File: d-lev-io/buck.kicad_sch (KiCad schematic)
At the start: 13 parts, among them U3 TPS54202DDC

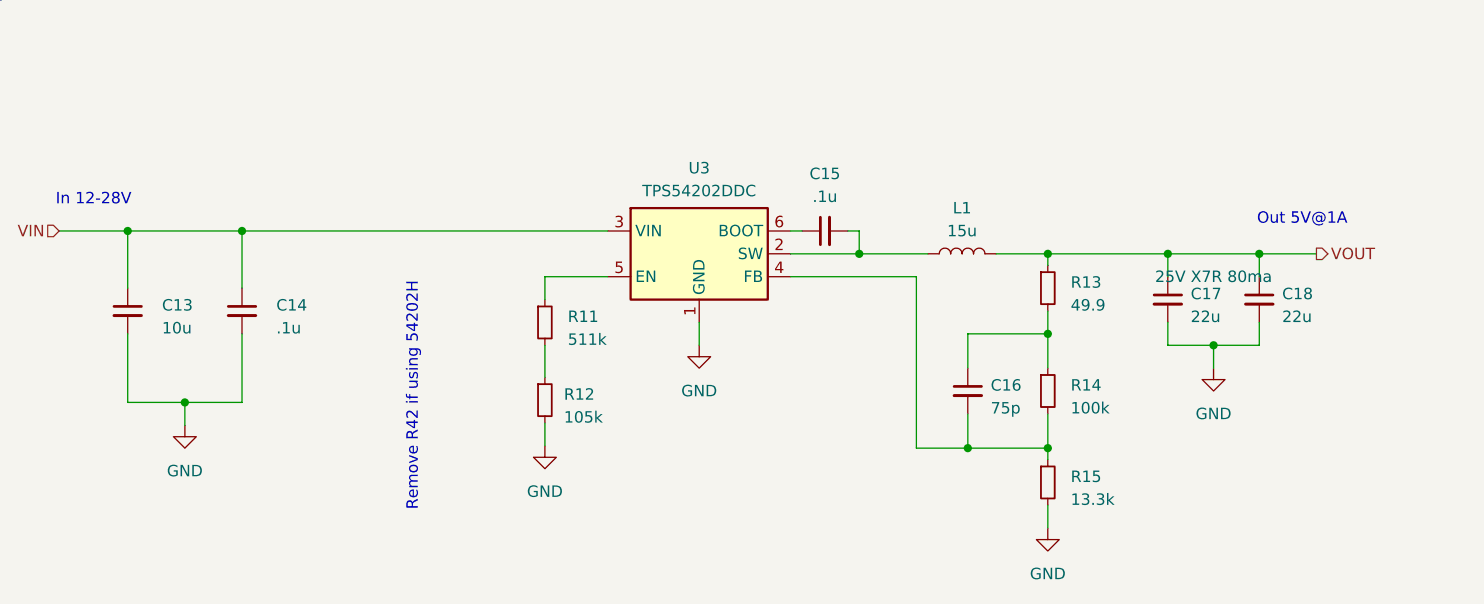
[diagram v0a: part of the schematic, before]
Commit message: I/O board silk placement
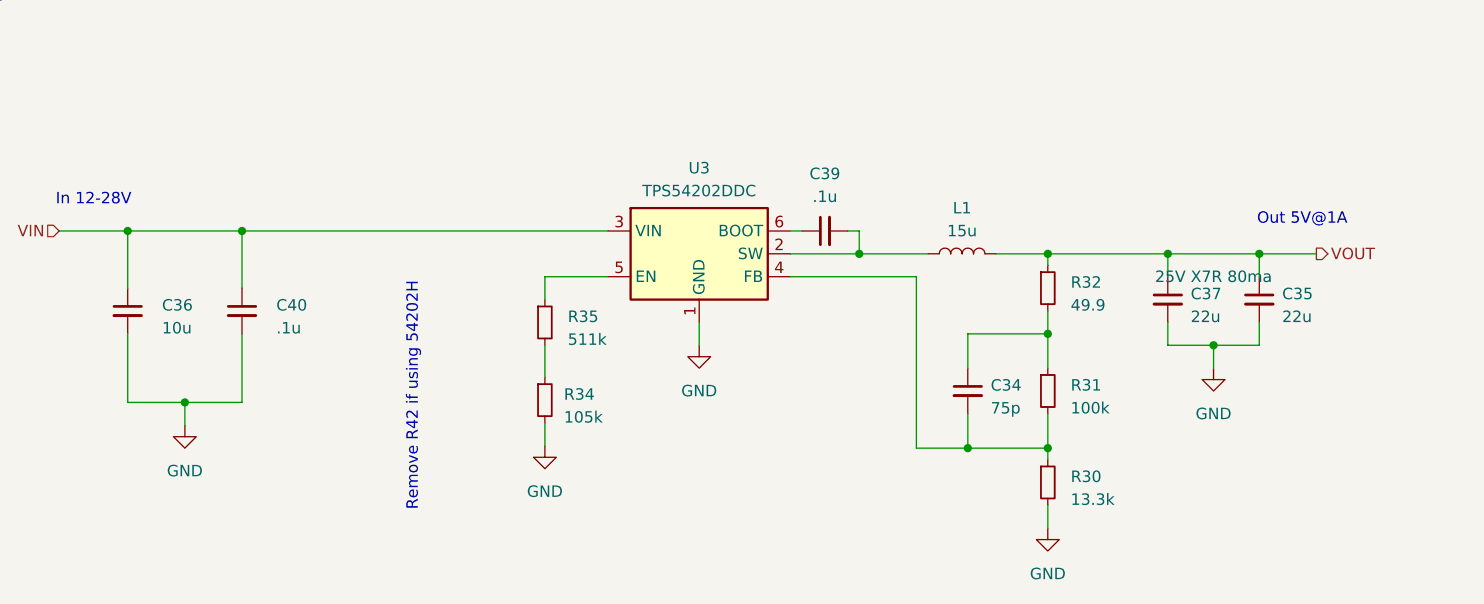
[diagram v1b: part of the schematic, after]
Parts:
- renumbered C16 to C34, C18 to C35, C13 to C36, C17 to C37, C15 to C39, C14 to C40, R15 to R30, R14 to R31, R13 to R32, R12 to R34, R11 to R35
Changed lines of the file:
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@@
   (symbol (lib_id "Device:R_Small") (at 193.675 110.49 0) (unit 1)
     (in_bom yes) (on_board yes) (dnp no) (fields_autoplaced)
-    (property "Reference" "R15" (at 196.215 109.855 0)
+    (property "Reference" "R30" (at 196.215 109.855 0)
       (effects (font (size 1.27 1.27)) (justify left))
     )
@@
       (project "d-lev-io"
         (path "/9261a07b-ae4a-4d72-8042-ea097cd0e5ed/f19ba83a-ef5a-459f-9ba4-5cb53e267077"
-          (reference "R15") (unit 1)
+          (reference "R30") (unit 1)
         )
       )
@@
   (symbol (lib_id "Device:R_Small") (at 193.675 88.9 0) (unit 1)
     (in_bom yes) (on_board yes) (dnp no) (fields_autoplaced)
-    (property "Reference" "R13" (at 196.215 88.265 0)
+    (property "Reference" "R32" (at 196.215 88.265 0)
       (effects (font (size 1.27 1.27)) (justify left))
     )
@@
       (project "d-lev-io"
         (path "/9261a07b-ae4a-4d72-8042-ea097cd0e5ed/f19ba83a-ef5a-459f-9ba4-5cb53e267077"
-          (reference "R13") (unit 1)
+          (reference "R32") (unit 1)
         )
       )
@@
   (symbol (lib_id "Device:C_Small") (at 184.785 100.33 0) (unit 1)
     (in_bom yes) (on_board yes) (dnp no)
-    (property "Reference" "C16" (at 187.325 99.7013 0)
+    (property "Reference" "C34" (at 187.325 99.7013 0)
       (effects (font (size 1.27 1.27)) (justify left))
     )
@@
       (project "d-lev-io"
         (path "/9261a07b-ae4a-4d72-8042-ea097cd0e5ed/f19ba83a-ef5a-459f-9ba4-5cb53e267077"
-          (reference "C16") (unit 1)
+          (reference "C34") (unit 1)
         )
       )
@@
   (symbol (lib_id "Device:C_Small") (at 104.14 91.44 0) (unit 1)
     (in_bom yes) (on_board yes) (dnp no) (fields_autoplaced)
-    (property "Reference" "C14" (at 107.95 90.805 0)
+    (property "Reference" "C40" (at 107.95 90.805 0)
       (effects (font (size 1.27 1.27)) (justify left))
     )
@@
       (project "d-lev-io"
         (path "/9261a07b-ae4a-4d72-8042-ea097cd0e5ed/f19ba83a-ef5a-459f-9ba4-5cb53e267077"
-          (reference "C14") (unit 1)
+          (reference "C40") (unit 1)
         )
       )
@@
   (symbol (lib_id "Device:C_Small") (at 91.44 91.44 0) (unit 1)
     (in_bom yes) (on_board yes) (dnp no) (fields_autoplaced)
-    (property "Reference" "C13" (at 95.25 90.805 0)
+    (property "Reference" "C36" (at 95.25 90.805 0)
       (effects (font (size 1.27 1.27)) (justify left))
     )
@@
       (project "d-lev-io"
         (path "/9261a07b-ae4a-4d72-8042-ea097cd0e5ed/f19ba83a-ef5a-459f-9ba4-5cb53e267077"
-          (reference "C13") (unit 1)
+          (reference "C36") (unit 1)
         )
       )
@@
   (symbol (lib_id "Device:R_Small") (at 193.675 100.33 0) (unit 1)
     (in_bom yes) (on_board yes) (dnp no) (fields_autoplaced)
-    (property "Reference" "R14" (at 196.215 99.695 0)
+    (property "Reference" "R31" (at 196.215 99.695 0)
       (effects (font (size 1.27 1.27)) (justify left))
     )
@@
       (project "d-lev-io"
         (path "/9261a07b-ae4a-4d72-8042-ea097cd0e5ed/f19ba83a-ef5a-459f-9ba4-5cb53e267077"
-          (reference "R14") (unit 1)
+          (reference "R31") (unit 1)
         )
       )
@@
   (symbol (lib_id "Device:C_Small") (at 207.01 90.17 0) (unit 1)
     (in_bom yes) (on_board yes) (dnp no)
-    (property "Reference" "C17" (at 209.55 89.5413 0)
+    (property "Reference" "C37" (at 209.55 89.5413 0)
       (effects (font (size 1.27 1.27)) (justify left))
     )
@@
       (project "d-lev-io"
         (path "/9261a07b-ae4a-4d72-8042-ea097cd0e5ed/f19ba83a-ef5a-459f-9ba4-5cb53e267077"
-          (reference "C17") (unit 1)
+          (reference "C37") (unit 1)
         )
       )
@@
   (symbol (lib_id "Device:R_Small") (at 137.795 101.346 0) (unit 1)
     (in_bom yes) (on_board yes) (dnp no) (fields_autoplaced)
-    (property "Reference" "R12" (at 139.9032 100.711 0)
+    (property "Reference" "R34" (at 139.9032 100.711 0)
       (effects (font (size 1.27 1.27)) (justify left))
     )
@@
       (project "d-lev-io"
         (path "/9261a07b-ae4a-4d72-8042-ea097cd0e5ed/f19ba83a-ef5a-459f-9ba4-5cb53e267077"
-          (reference "R12") (unit 1)
+          (reference "R34") (unit 1)
         )
       )
@@
   (symbol (lib_id "Device:C_Small") (at 168.91 82.55 90) (unit 1)
     (in_bom yes) (on_board yes) (dnp no) (fields_autoplaced)
-    (property "Reference" "C15" (at 168.91 76.2 90)
+    (property "Reference" "C39" (at 168.91 76.2 90)
       (effects (font (size 1.27 1.27)))
     )
@@
       (project "d-lev-io"
         (path "/9261a07b-ae4a-4d72-8042-ea097cd0e5ed/f19ba83a-ef5a-459f-9ba4-5cb53e267077"
-          (reference "C15") (unit 1)
+          (reference "C39") (unit 1)
         )
       )
@@
   (symbol (lib_id "Device:C_Small") (at 217.17 90.17 0) (unit 1)
     (in_bom yes) (on_board yes) (dnp no)
-    (property "Reference" "C18" (at 219.71 89.5413 0)
+    (property "Reference" "C35" (at 219.71 89.5413 0)
       (effects (font (size 1.27 1.27)) (justify left))
     )
@@
       (project "d-lev-io"
         (path "/9261a07b-ae4a-4d72-8042-ea097cd0e5ed/f19ba83a-ef5a-459f-9ba4-5cb53e267077"
-          (reference "C18") (unit 1)
+          (reference "C35") (unit 1)
         )
       )
@@
         )
         (path "/9261a07b-ae4a-4d72-8042-ea097cd0e5ed/f19ba83a-ef5a-459f-9ba4-5cb53e267077"
-          (reference "U2") (unit 1)
+          (reference "U7") (unit 1)
         )
       )
@@
   (symbol (lib_id "Device:R_Small") (at 137.795 92.71 0) (unit 1)
     (in_bom yes) (on_board yes) (dnp no) (fields_autoplaced)
-    (property "Reference" "R11" (at 140.335 92.075 0)
+    (property "Reference" "R35" (at 140.335 92.075 0)
       (effects (font (size 1.27 1.27)) (justify left))
     )
@@
       (project "d-lev-io"
         (path "/9261a07b-ae4a-4d72-8042-ea097cd0e5ed/f19ba83a-ef5a-459f-9ba4-5cb53e267077"
-          (reference "R11") (unit 1)
-        )
-      )
+          (reference "R35") (unit 1)
+        )
+      )

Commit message: Add iBOMs and additional part numbers
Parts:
- C34: MPN (none) -> 0603N750J500CT; Notes (none) -> Common; Supplier (none) -> Digi-Key; Supplier URL (none) -> https://www.digikey.com/en/products/detail/walsin-technolog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
- C35, C37: Notes (none) -> 25V X7R 80ma; Supplier (none) -> Mouser; Supplier URL (none) -> https://www.mouser.com/ProductDetail/187-CL32B226KAJNNNE; Voltage 25V X7R 80ma -> (none)
- C36: Notes (none) -> 30V 2A X5R; Supplier (none) -> Mouser; Supplier URL (none) -> https://www.mouser.com/ProductDetail/187-CL32B106KAJNFNE; Voltage 30V 2A X5R -> (none)
- C39: value .1u -> 100n; Supplier (none) -> Mouser; Supplier URL (none) -> https://www.mouser.com/ProductDetail/581-08053C104MAT4A; Voltage 30V -> (none)
- C40: value .1u -> 100n; Supplier (none) -> Mouser; Supplier URL (none) -> https://www.mouser.com/ProductDetail/581-08053C104MAT4A; Voltage 30V 2A -> (none)
- L1: MPN (none) -> SRN8040TA-150M; Supplier (none) -> Mouser; Supplier URL (none) -> https://www.mouser.com/ProductDetail/652-SRN8040TA-150M
- R30: MPN (none) -> CRCW080513K3FKEA; Supplier (none) -> Mouser; Supplier URL (none) -> https://www.mouser.com/ProductDetail/71-CRCW0805-13.3K-E3
- R31: MPN (none) -> WR08X1003FTL; Supplier (none) -> Digi-Key; Supplier URL (none) -> https://www.digikey.com/en/products/detail/walsin-technolog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
- R32: MPN (none) -> RC0805FR-0749R9L; Supplier (none) -> Digi-Key; Supplier URL (none) -> https://www.digikey.com/en/products/detail/yageo/RC0805FR-0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
- R34: MPN (none) -> CR0603-FX1053ELF; Supplier (none) -> Mouser; Supplier URL (none) -> https://www.mouser.com/ProductDetail/652-CR0603-FX1053ELF
- R35: MPN (none) -> CR0603FX-5113ELF; Supplier (none) -> Mouser; Supplier URL (none) -> https://www.mouser.com/ProductDetail/652-CR0603FX-5113ELF
- U3: MPN (none) -> TPS54202DDCR; Supplier (none) -> Mouser; Supplier URL (none) -> https://www.mouser.com/ProductDetail/595-TPS54202DDCR
